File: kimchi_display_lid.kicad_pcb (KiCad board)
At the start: 4 copper layers, 147 x 77 mm, 13 parts, among them J1 DF40HC(3.5)-60DS, J2 DF40HC(3.5)-60DS, U1 24C32

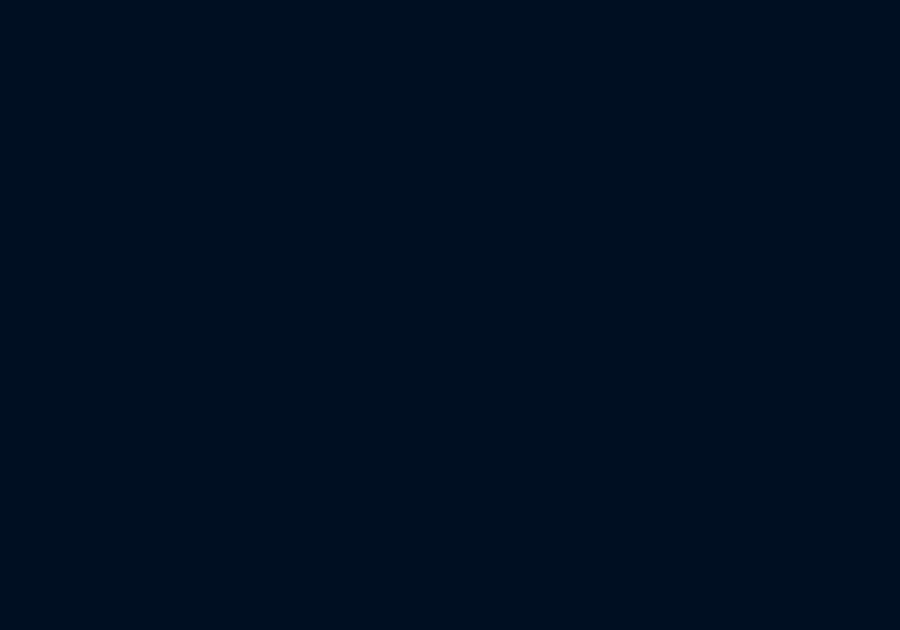
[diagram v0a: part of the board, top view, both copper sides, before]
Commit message: Add LCD backlight LED driver
Signed-off-by: Michael Welling <mwelling@ieee.org>
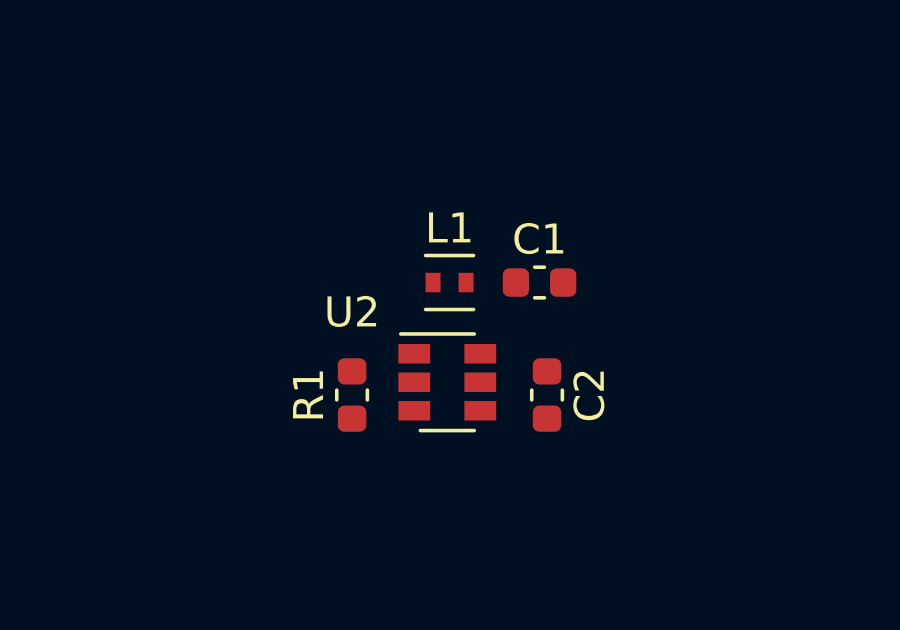
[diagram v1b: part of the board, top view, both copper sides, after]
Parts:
- removed REF**: kimchi-micro-3d-model, kimchi_ulid:kimchi-micro-3d-model
- added C1: 1uF, Capacitor_SMD:C_0603_1608Metric, F.Cu at (136.8, 80.5)
- added C2: 0.22uF 50V, Capacitor_SMD:C_0603_1608Metric, F.Cu at (137.0, 84.2)
- added L1: 22uH, Inductor_SMD:L_Taiyo-Yuden_MD-1616, F.Cu at (133.8, 80.5)
- added R1: 10 1%, Resistor_SMD:R_0603_1608Metric, F.Cu at (130.5, 84.2)
- added U2: AP3019AKTR-G1, Package_TO_SOT_SMD:SOT-23-6, F.Cu at (133.7, 83.8)

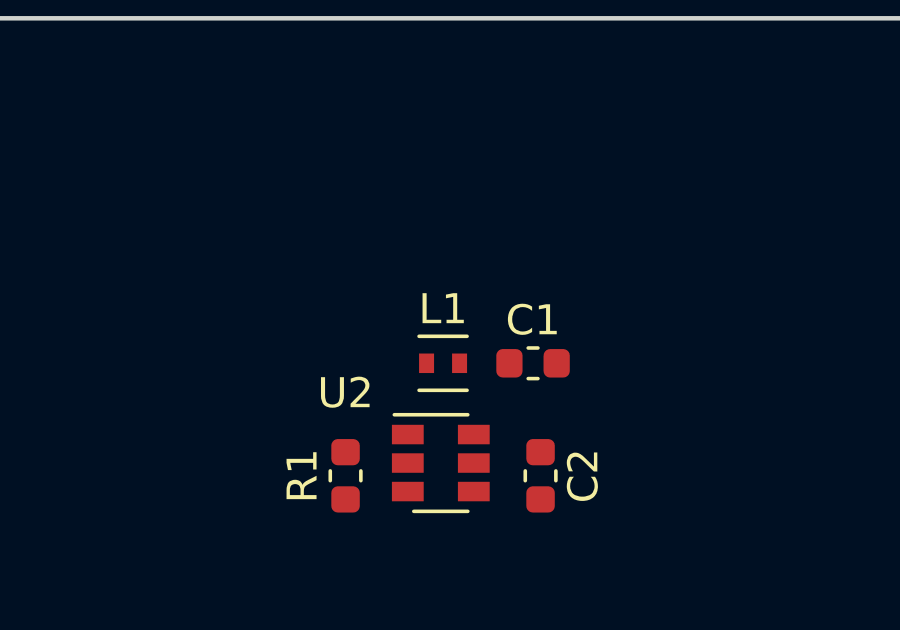
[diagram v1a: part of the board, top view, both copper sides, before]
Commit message: Bump inductor to a big package
Signed-off-by: Michael Welling <mwelling@ieee.org>
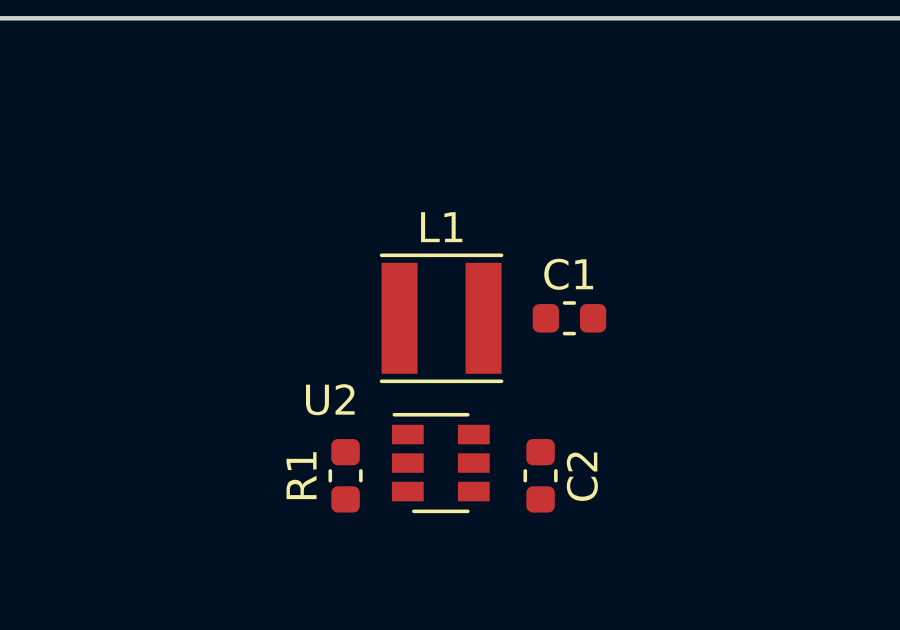
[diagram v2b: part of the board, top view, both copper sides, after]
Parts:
- L1: footprint Inductor_SMD:L_Taiyo-Yuden_MD-1616 -> Inductor_SMD:L_Taiyo-Yuden_MD-4040
- moved C1 1.93 mm to (138.0, 79.0)
- moved L1 1.50 mm to (133.7, 79.0)
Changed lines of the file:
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@@
     (diff_pair_width 0.101346)
   )
+  (module Inductor_SMD:L_Taiyo-Yuden_MD-4040 (layer F.Cu)
+    (at 133.7 79)
+    (descr "Inductor, Taiyo Yuden, MD series, Taiyo-Yuden_MD-4040, 4.0mmx4.0mm")
+    (tags "inductor taiyo-yuden md smd")
+    (attr smd)
+    (fp_text reference L1 (at 0 -3) (layer F.SilkS)
+      (effects (font (size 1 1) (thickness 0.15)))
+    )
+    (fp_text value 22uH (at 0 3.5) (layer F.Fab)
+      (effects (font (size 1 1) (thickness 0.15)))
+    )
+    (fp_text user %R (at 0 0) (layer F.Fab)
+      (effects (font (size 1 1) (thickness 0.15)))
+    )
+    (fp_line (start -2 -2) (end -2 2) (layer F.Fab) (width 0.1))
+    (fp_line (start -2 2) (end 2 2) (layer F.Fab) (width 0.1))
+    (fp_line (start 2 2) (end 2 -2) (layer F.Fab) (width 0.1))
+    (fp_line (start 2 -2) (end -2 -2) (layer F.Fab) (width 0.1))
+    (fp_line (start -2 -2.1) (end 2 -2.1) (layer F.SilkS) (width 0.12))
+    (fp_line (start -2 2.1) (end 2 2.1) (layer F.SilkS) (width 0.12))
+    (fp_line (start -2.25 -2.25) (end -2.25 2.25) (layer F.CrtYd) (width 0.05))
+    (fp_line (start -2.25 2.25) (end 2.25 2.25) (layer F.CrtYd) (width 0.05))
+    (fp_line (start 2.25 2.25) (end 2.25 -2.25) (layer F.CrtYd) (width 0.05))
+    (fp_line (start 2.25 -2.25) (end -2.25 -2.25) (layer F.CrtYd) (width 0.05))
+    (pad 1 smd rect (at -1.4 0) (size 1.2 3.7) (layers F.Cu F.Paste F.Mask)
+      (net 101 "Net-(L1-Pad1)"))
+    (pad 2 smd rect (at 1.4 0) (size 1.2 3.7) (layers F.Cu F.Paste F.Mask)
+      (net 4 VDD_3V3))
+    (model ${KISYS3DMOD}/Inductor_SMD.3dshapes/L_Taiyo-Yuden_MD-4040.wrl
+      (at (xyz 0 0 0))
+      (scale (xyz 1 1 1))
+      (rotate (xyz 0 0 0))
+    )
+  )
   (module Capacitor_SMD:C_0603_1608Metric (layer F.Cu)
-    (at 136.75 80.5)
+    (at 137.9625 79)
     (descr "Capacitor SMD 0603 (1608 Metric), square (rectangular) end terminal, IPC_7351 nominal, (Body size source: http://www.tortai-tech.com/upload/download/2011102023233369053.pdf), generated with kicad-footprint-generator")
     (tags capacitor)
@@
     )
   )
-  (module Inductor_SMD:L_Taiyo-Yuden_MD-1616 (layer F.Cu)
-    (at 133.75 80.5)
-    (descr "Inductor, Taiyo Yuden, MD series, Taiyo-Yuden_MD-1616, 1.6mmx1.6mm")
-    (tags "inductor taiyo-yuden md smd")
-    (attr smd)
-    (fp_text reference L1 (at 0 -1.8) (layer F.SilkS)
-      (effects (font (size 1 1) (thickness 0.15)))
-    )
-    (fp_text value 22uH (at 0 2.3) (layer F.Fab)
-      (effects (font (size 1 1) (thickness 0.15)))
-    )
-    (fp_text user %R (at 0 0) (layer F.Fab)
-      (effects (font (size 0.3 0.3) (thickness 0.05)))
-    )
-    (fp_line (start -0.8 -0.8) (end -0.8 0.8) (layer F.Fab) (width 0.1))
-    (fp_line (start -0.8 0.8) (end 0.8 0.8) (layer F.Fab) (width 0.1))
-    (fp_line (start 0.8 0.8) (end 0.8 -0.8) (layer F.Fab) (width 0.1))
-    (fp_line (start 0.8 -0.8) (end -0.8 -0.8) (layer F.Fab) (width 0.1))
-    (fp_line (start -0.8 -0.9) (end 0.8 -0.9) (layer F.SilkS) (width 0.12))
-    (fp_line (start -0.8 0.9) (end 0.8 0.9) (layer F.SilkS) (width 0.12))
-    (fp_line (start -1.1 -1.1) (end -1.1 1.1) (layer F.CrtYd) (width 0.05))
-    (fp_line (start -1.1 1.1) (end 1.1 1.1) (layer F.CrtYd) (width 0.05))
-    (fp_line (start 1.1 1.1) (end 1.1 -1.1) (layer F.CrtYd) (width 0.05))
-    (fp_line (start 1.1 -1.1) (end -1.1 -1.1) (layer F.CrtYd) (width 0.05))
-    (pad 1 smd rect (at -0.55 0) (size 0.5 0.65) (layers F.Cu F.Paste F.Mask)
-      (net 101 "Net-(L1-Pad1)"))
-    (pad 2 smd rect (at 0.55 0) (size 0.5 0.65) (layers F.Cu F.Paste F.Mask)
-      (net 4 VDD_3V3))
-    (model ${KISYS3DMOD}/Inductor_SMD.3dshapes/L_Taiyo-Yuden_MD-1616.wrl
-      (at (xyz 0 0 0))
-      (scale (xyz 1 1 1))
-      (rotate (xyz 0 0 0))
-    )
-  )
   (module Package_TO_SOT_SMD:SOT-23-6 (layer F.Cu)
     (at 133.675001 83.825001)
@@
     (tags SOT-23-6)
     (attr smd)
-    (fp_text reference U2 (at -3.175001 -2.325001) (layer F.SilkS)
+    (fp_text reference U2 (at -3.675001 -2.075001) (layer F.SilkS)
       (effects (font (size 1 1) (thickness 0.15)))
     )

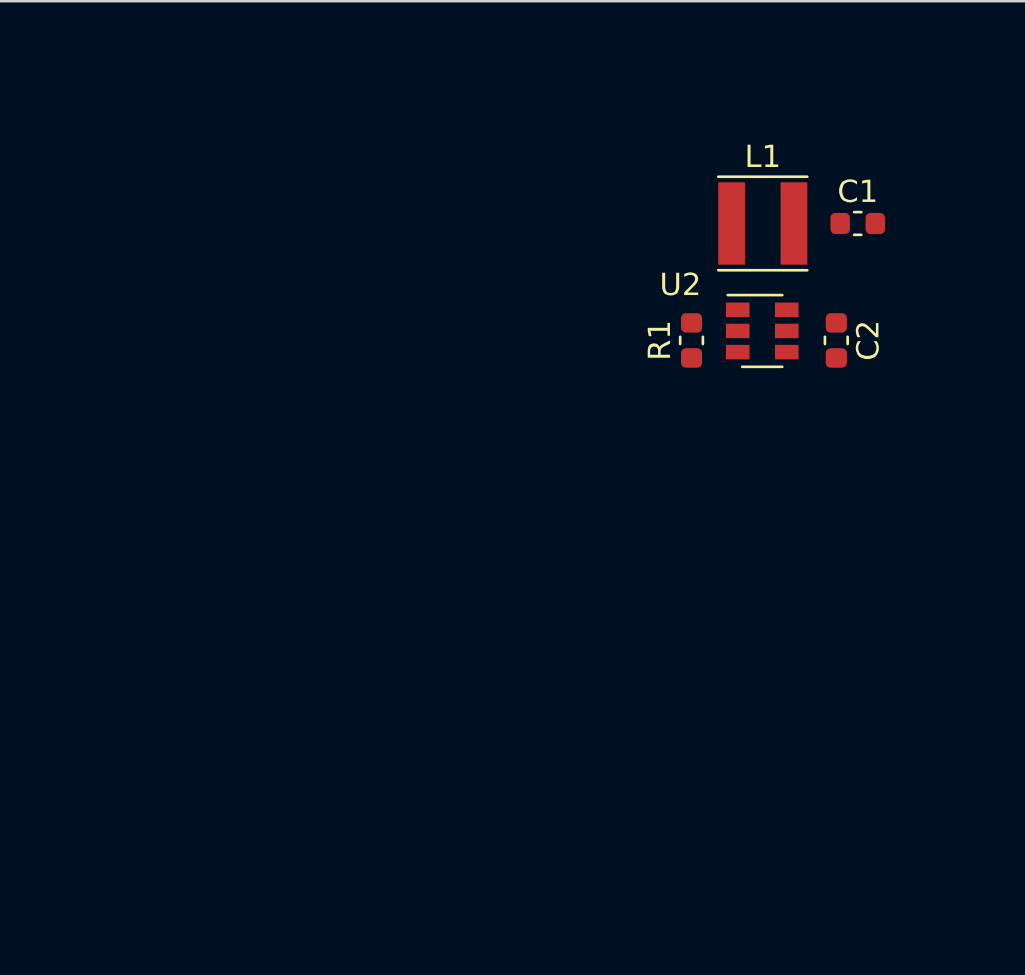
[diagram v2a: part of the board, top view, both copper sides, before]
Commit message: Add LCD connectors to the schematic / PCB
Signed-off-by: Michael Welling <mwelling@ieee.org>
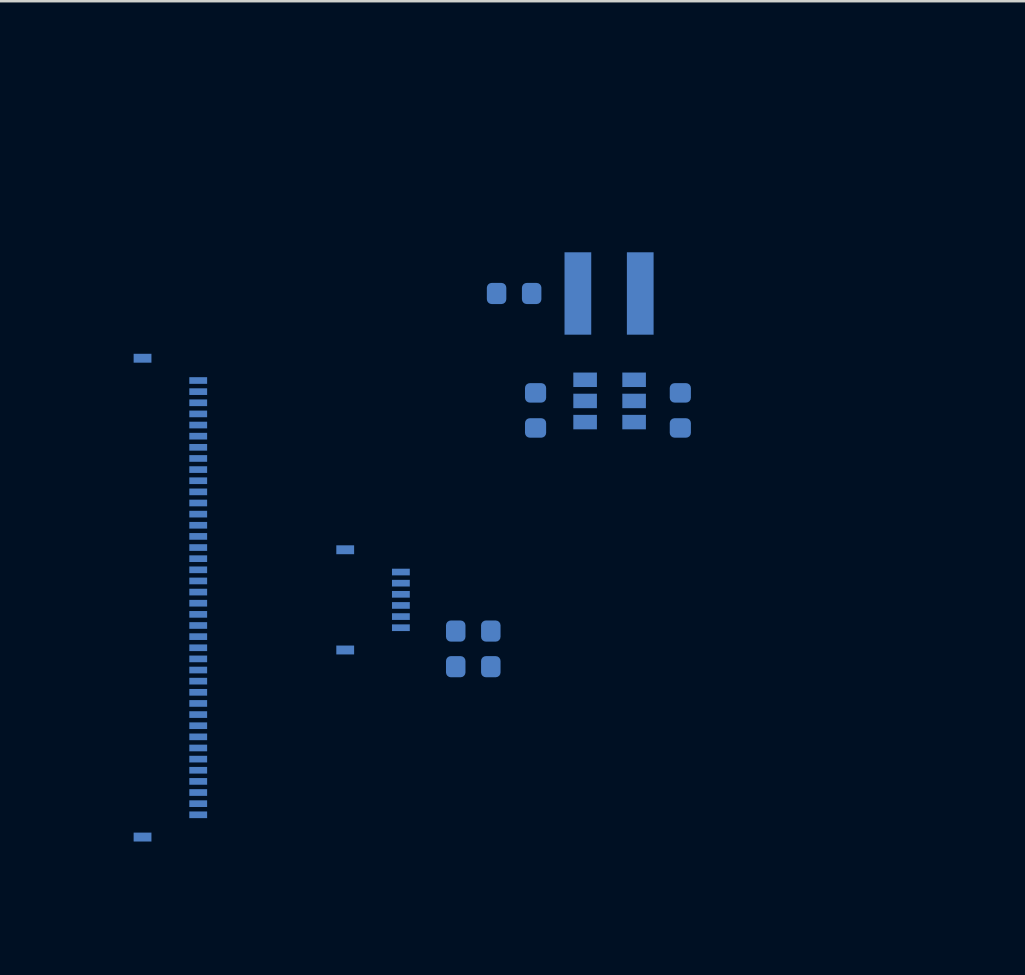
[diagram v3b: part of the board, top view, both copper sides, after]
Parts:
- added J3: H19C-6S-0.5SH, kimchi_ulid:HRS_FH19C-6S-0.5SH_1x06-1MP_P0.50mm, B.Cu at (116.2, 95.9)
- added J4: FH19C-40S-0.5SH(10), kimchi_ulid:HRS_FH19C-40S-0.5SH_1x40-1MP_P0.50mm, B.Cu at (107.1, 95.8)
- added LOGO2: Logo_Open_Hardware_Small, kimchi_ulid:kimchi-micro-3d-model, B.Cu at (134.5, 128.0)
- added R2: 4.7K, Resistor_SMD:R_0603_1608Metric, B.Cu at (120.7, 98.9)
- added R3: 4.7K, Resistor_SMD:R_0603_1608Metric, B.Cu at (120.7, 97.3)
- C1, C2, L1, R1, U2: moved to B.Cu
- moved C1 15.7 mm to (122.5, 82.1), turned to 180 degrees
- moved C2 13.9 mm to (123.5, 87.4)
- moved L1 7.58 mm to (126.8, 82.1), turned to 180 degrees
- moved U2 7.54 mm to (126.8, 87.0), turned to 180 degrees
- moved R1 3.18 mm to (130.0, 87.4)

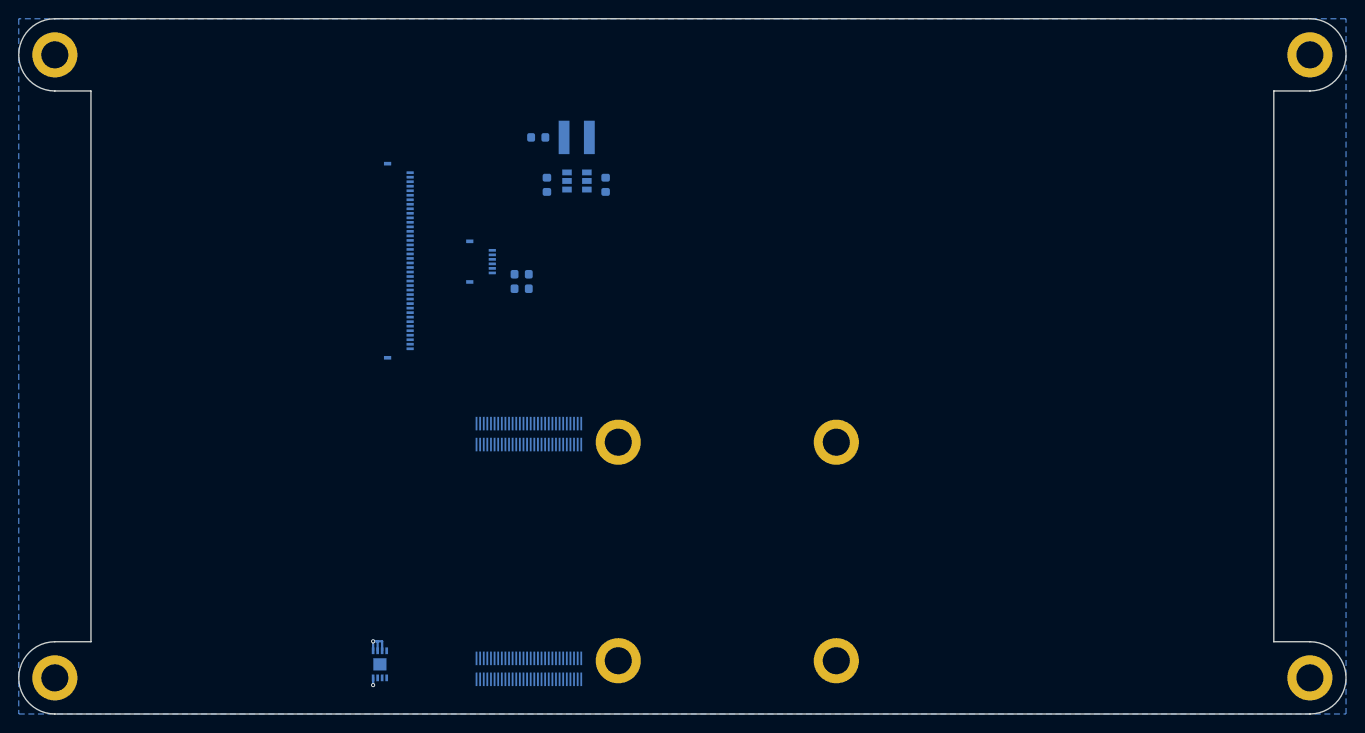
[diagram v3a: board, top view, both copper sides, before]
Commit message: Update placement of FPC connectors and kimx module
Should be close enough.

Signed-off-by: Michael Welling <mwelling@ieee.org>
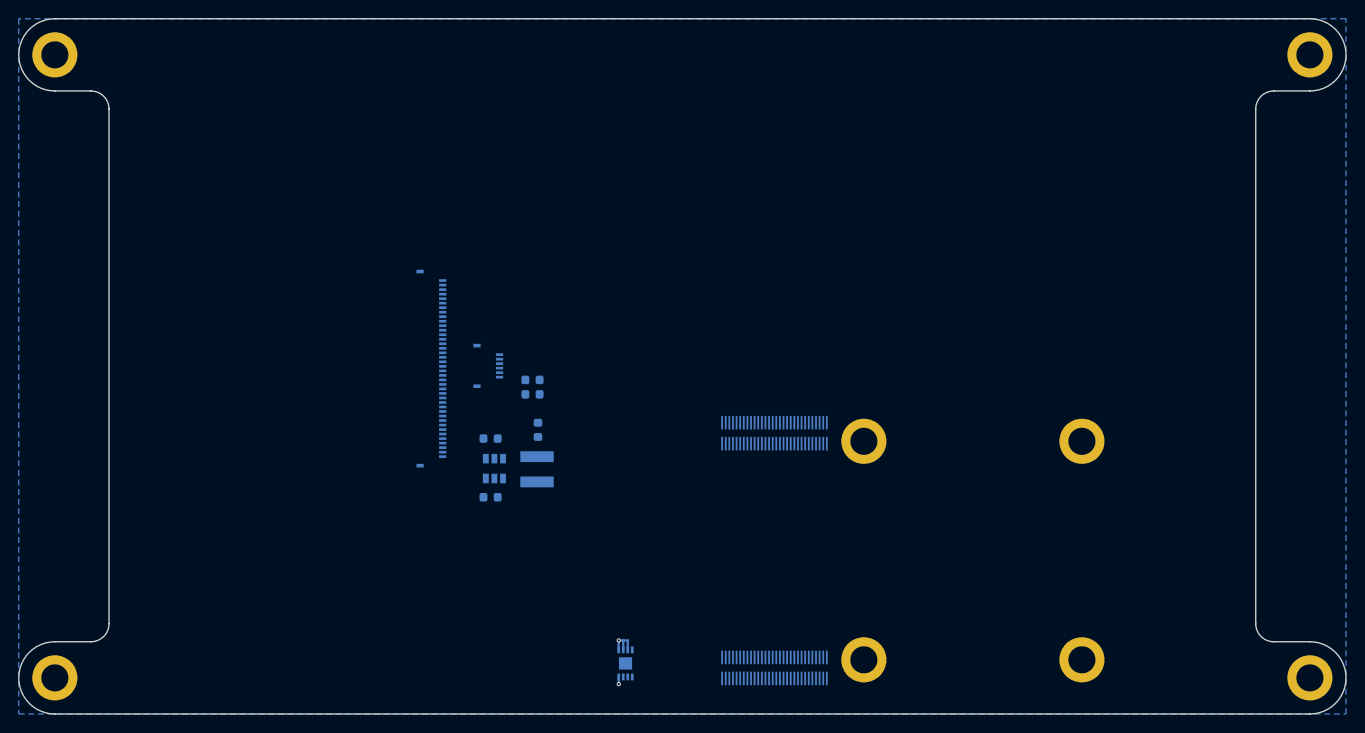
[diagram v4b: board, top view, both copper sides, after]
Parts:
- moved L1 37.0 mm to (122.4, 118.9), turned to 90 degrees
- moved R1 36.9 mm to (117.3, 122.0), turned to 0 degrees
- moved U2 33.1 mm to (117.7, 118.8), turned to 90 degrees
- moved C1 32.4 mm to (122.5, 114.5), turned to 90 degrees
- moved C2 28.8 mm to (117.3, 115.5), turned to 180 degrees
- moved H1 27.2 mm to (182.8, 140.0)
- moved H2 27.2 mm to (182.8, 115.8)
- moved H3 27.2 mm to (158.6, 140.0)
- moved H4 27.2 mm to (158.6, 115.8)
- moved J1 27.2 mm to (148.7, 140.9)
- moved J2 27.2 mm to (148.7, 114.9)
- moved LOGO2 27.2 mm to (161.7, 127.9)
- moved U1 27.2 mm to (132.2, 140.4)
- moved J4 12.5 mm to (110.7, 107.8)
- moved R3 11.8 mm to (121.9, 109.0)
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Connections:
- J3 pad 1: I2C3_SDA -> GND
- J3 pad 2: I2C3_SCL -> VDD_3V3
- J3 pad 3: /TS_RESET -> /TS_INT
- J3 pad 4: /TS_INT -> /TS_RESET
- J3 pad 5: VDD_3V3 -> I2C3_SCL
- J3 pad 6: GND -> I2C3_SDA
- J4 pad 1: Net-(J4-Pad1) -> /VLED-
- J4 pad 10: VDD_3V3 -> /DISP_D1_P
- J4 pad 11: VDD_3V3 -> GND
- J4 pad 12: Net-(J4-Pad12) -> /DISP_CK_N
- J4 pad 13: Net-(J4-Pad13) -> /DISP_CK_P
- J4 pad 14: /LCD_RESET -> GND
- J4 pad 15: /LCD_TE -> /DISP_D2_N
- J4 pad 16: Net-(J4-Pad16) -> /DISP_D2_P
- J4 pad 18: GND -> /DISP_D3_N
- J4 pad 19: VDD_3V3 -> /DISP_D3_P
- J4 pad 2: Net-(J4-Pad2) -> /VLED-
- J4 pad 20: VDD_3V3 -> GND
- J4 pad 21: GND -> VDD_3V3
- J4 pad 22: /DISP_D3_P -> VDD_3V3
- J4 pad 23: /DISP_D3_N -> GND
- J4 pad 25: /DISP_D2_P -> Net-(J4-Pad25)
- J4 pad 26: /DISP_D2_N -> /LCD_TE
- J4 pad 27: GND -> /LCD_RESET
- J4 pad 28: /DISP_CK_P -> Net-(J4-Pad28)
- J4 pad 29: /DISP_CK_N -> Net-(J4-Pad29)
- J4 pad 3: Net-(J4-Pad3) -> /VLED+
- J4 pad 30: GND -> VDD_3V3
- J4 pad 31: /DISP_D1_P -> VDD_3V3
- J4 pad 32: /DISP_D1_N -> Net-(J4-Pad32)
- J4 pad 33: GND -> Net-(J4-Pad33)
- J4 pad 34: /DISP_D0_P -> Net-(J4-Pad34)
- J4 pad 35: /DISP_D0_N -> Net-(J4-Pad35)
- J4 pad 36: GND -> Net-(J4-Pad36)
- J4 pad 37: GND -> Net-(J4-Pad37)
- J4 pad 38: /VLED+ -> Net-(J4-Pad38)
- J4 pad 39: /VLED- -> Net-(J4-Pad39)
- J4 pad 4: Net-(J4-Pad4) -> GND
- J4 pad 40: /VLED- -> Net-(J4-Pad40)
- J4 pad 5: Net-(J4-Pad5) -> GND
- J4 pad 6: Net-(J4-Pad6) -> /DISP_D0_N
- J4 pad 7: Net-(J4-Pad7) -> /DISP_D0_P
- J4 pad 8: Net-(J4-Pad8) -> GND
- J4 pad 9: Net-(J4-Pad9) -> /DISP_D1_N
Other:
- outline, holes or cut-outs redrawn
- board text added: "FPC PIN 1 ->"
